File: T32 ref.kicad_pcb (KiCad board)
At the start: 4 copper layers, 71.1 x 25.4 mm, 89 parts, among them K1 MK20DX256VLH7, K2 MKL04Z32VLC4, T1 MCP1825S, X1 MINI-USB

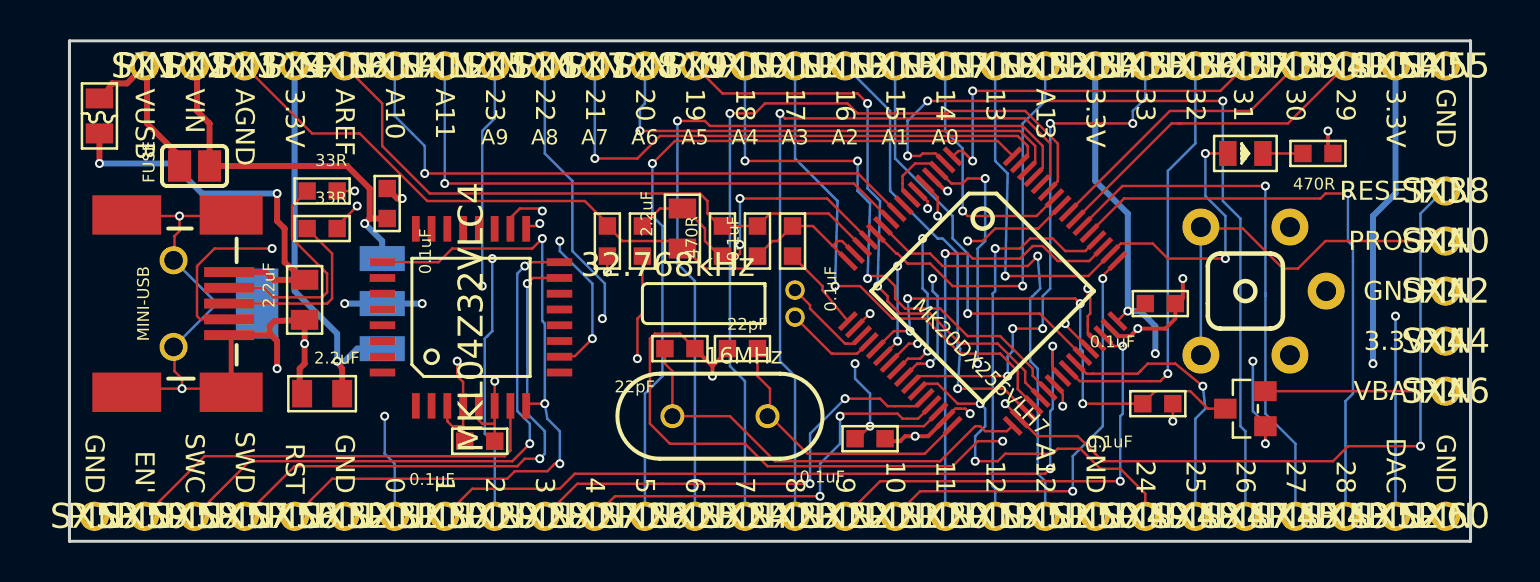
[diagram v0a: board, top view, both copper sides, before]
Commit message: Convert to new library format and fix DRC errors
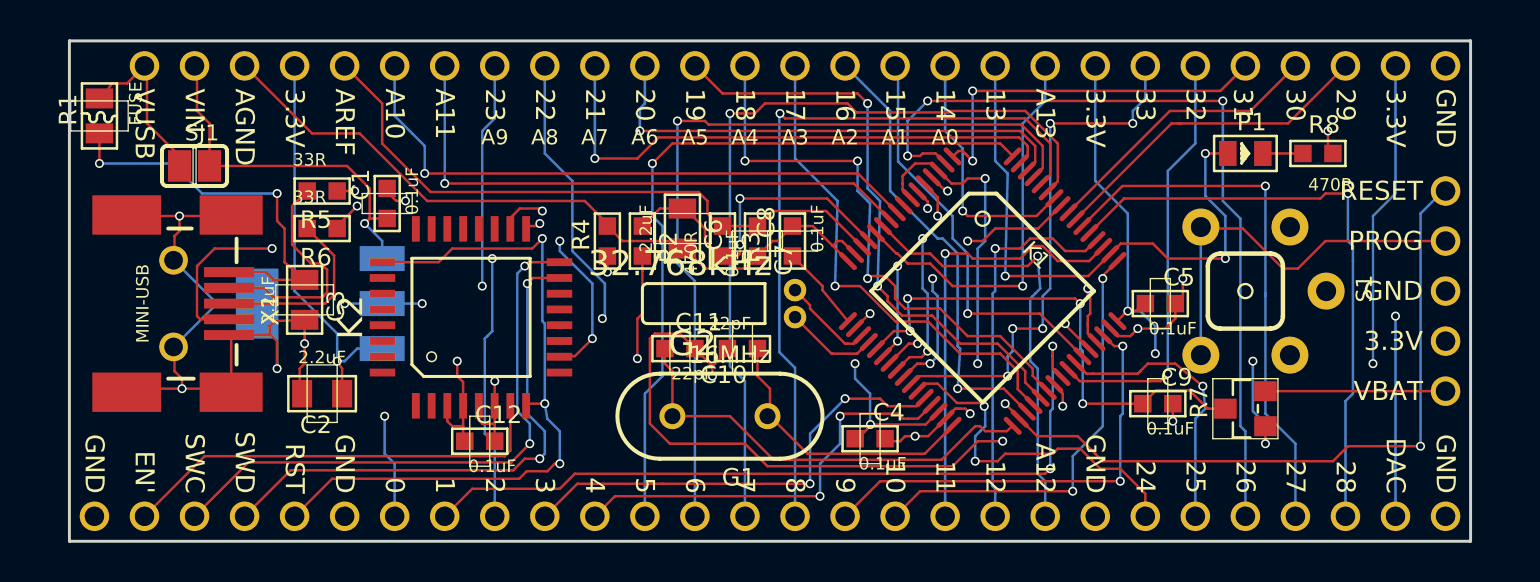
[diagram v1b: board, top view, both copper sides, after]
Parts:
- C1, C10, C11, C12, C4, C5, C7, C8, C9: footprint C0603 -> T32 ref:C0603
- C2, C3, C6: footprint C0805 -> T32 ref:C0805
- G1: footprint HC49US -> T32 ref:HC49US
- G2: footprint TC26H -> T32 ref:TC26H
- K1: footprint LQFP64-05 -> T32 ref:LQFP64-05
- K2: footprint LQFP32-08 -> T32 ref:LQFP32-08
- P1: footprint LED-0805 -> T32 ref:LED-0805
- R1: footprint F0805 -> T32 ref:F0805
- R2, R4: footprint L0603 -> T32 ref:L0603
- R3, R5, R6, R8: footprint R0603 -> T32 ref:R0603
- R7: footprint SOT-23 -> T32 ref:SOT-23
- S1: footprint ALPS_SKHH -> T32 ref:ALPS_SKHH
- SJ1: footprint SOLDERJUMPER -> T32 ref:SOLDERJUMPER
- SX1, SX10, SX11, SX12, SX13, SX14, SX15, SX16, SX17, SX18, SX19, SX2, SX20, SX21, SX22, SX23, SX24, SX25, SX26, SX27, SX28, SX29, SX3, SX30, SX31, SX32, SX33, SX34, SX35, SX36, SX37, SX38, SX39, SX4, SX40, SX41, SX42, SX43, SX44, SX45, SX46, SX47, SX48, SX49, SX5, SX50, SX51, SX52, SX53, SX54, SX55, SX56, SX57, SX58, SX59, SX6, SX60, SX7, SX8, SX9: footprint PTH_39MIL -> T32 ref:PTH_39MIL
- T1: footprint SOT-223 -> T32 ref:SOT-223
- X1: footprint MOLEX_SD-67503-010 -> T32 ref:MOLEX_SD-67503-010
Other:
- net class Default: via_dia 0.6 -> 0.457; via_drill 0.4 -> 0.3

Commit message: Replace common footprints with KiCad versions
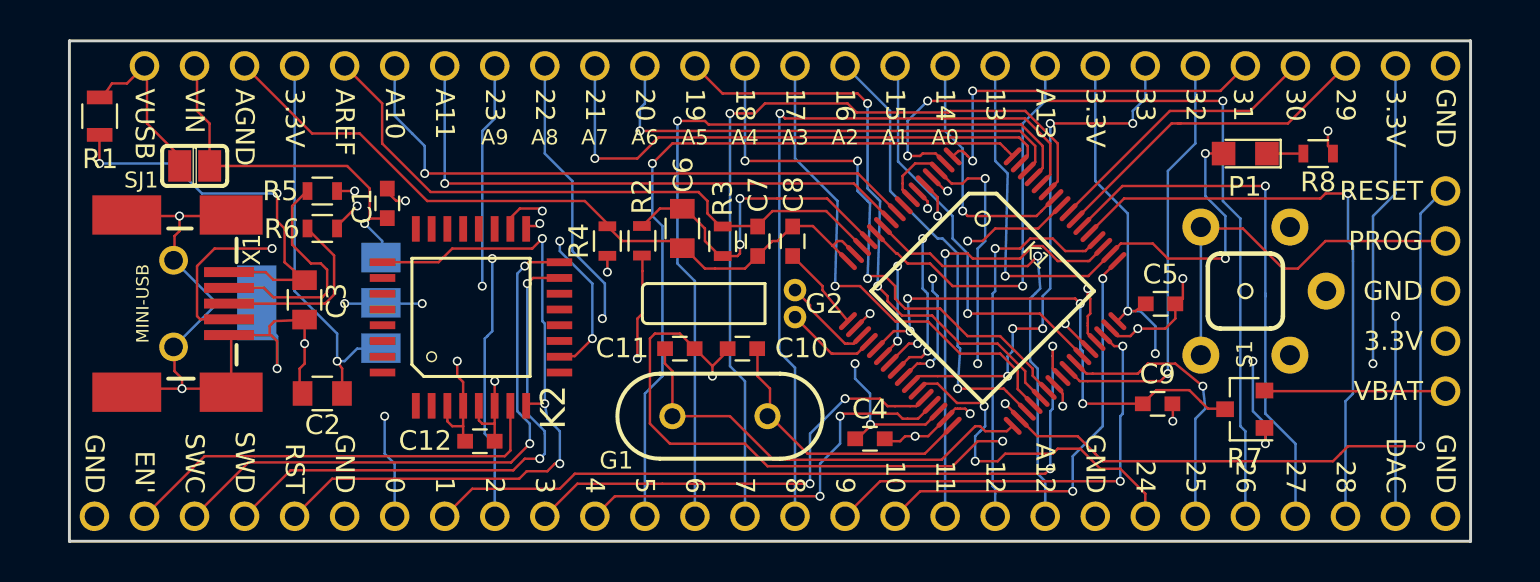
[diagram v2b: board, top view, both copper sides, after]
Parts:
- C1, C10, C11, C12, C4, C5, C7, C8, C9: footprint T32 ref:C0603 -> Capacitors_SMD:C_0603
- C2, C3, C6: footprint T32 ref:C0805 -> Capacitors_SMD:C_0805
- P1: footprint T32 ref:LED-0805 -> LEDs:LED_0805
- R1: footprint T32 ref:F0805 -> Resistors_SMD:R_0805
- R2, R4: footprint T32 ref:L0603 -> Resistors_SMD:R_0603
- R3, R5, R6, R8: footprint T32 ref:R0603 -> Resistors_SMD:R_0603
- R7: footprint T32 ref:SOT-23 -> TO_SOT_Packages_SMD:SOT-23
- T1: footprint T32 ref:SOT-223 -> TO_SOT_Packages_SMD:SOT-223
- moved T1 0.06 mm to (125.6, 105.6), turned to 180 degrees
- turned R7 to 180 degrees
- turned C5 to 0 degrees
- turned R3 to 90 degrees
- turned R1 to 90 degrees
- turned C7 to 270 degrees
- turned C8 to 90 degrees
- turned C9 to 0 degrees
- turned C2 to 180 degrees
- turned R8 to 180 degrees
- turned C1 to 90 degrees
- turned P1 to 180 degrees
- turned R6 to 0 degrees
- turned C6 to 270 degrees
- turned R5 to 0 degrees
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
